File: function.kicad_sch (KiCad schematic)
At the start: 0 parts

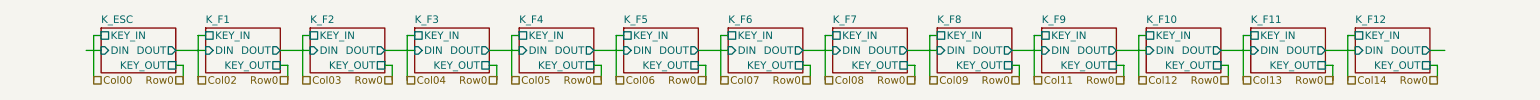
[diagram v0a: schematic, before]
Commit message: Unified key sch pages
One large page is simpler in this case
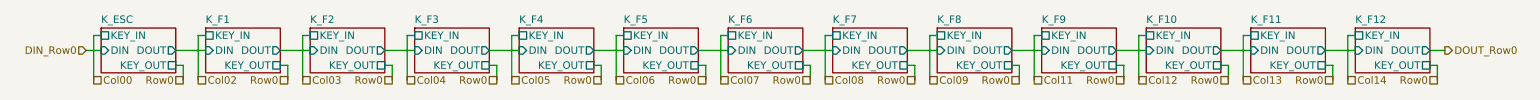
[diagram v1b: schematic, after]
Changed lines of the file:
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@@
+		)
+	)
+	(hierarchical_label "DIN_Row0"
+		(shape input)
+		(at 33.02 106.68 180)
+		(effects
+			(font
+				(size 1.27 1.27)
+			)
+			(justify right)
 		)
 	)
@@
 		(effects
 			(font
+				(size 1.27 1.27)
+			)
+			(justify left)
+		)
+	)
+	(hierarchical_label "DOUT_Row0"
+		(shape output)
+		(at 264.16 106.68 0)
+		(effects
+			(font
